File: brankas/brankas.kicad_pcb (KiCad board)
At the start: 2 copper layers, 1 part, among them SW1 SW_SPDT_XKB_DMx-xxxx-1

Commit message: Add Track
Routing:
- net unconnected-(SW1-A-Pad1): track 0.00 -> 157.9 mm
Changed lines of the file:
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@@
 		)
 	)
+	(segment
+		(start 177 78)
+		(end 208 47)
+		(width 0.2)
+		(layer "F.Cu")
+		(net 2)
+	)
+	(segment
+		(start 137.5 36.5)
+		(end 119 55)
+		(width 0.2)
+		(layer "F.Cu")
+		(net 2)
+	)
+	(segment
+		(start 164 78)
+		(end 177 78)
+		(width 0.2)
+		(layer "F.Cu")
+		(net 2)
+	)
+	(segment
+		(start 197.5 36.5)
+		(end 173.5 36.5)
+		(width 0.2)
+		(layer "F.Cu")
+		(net 2)
+	)
+	(segment
+		(start 173.5 36.5)
+		(end 137.5 36.5)
+		(width 0.2)
+		(layer "F.Cu")
+		(net 2)
+	)
+	(segment
+		(start 208 47)
+		(end 197.5 36.5)
+		(width 0.2)
+		(layer "F.Cu")
+		(net 2)
+	)
 )

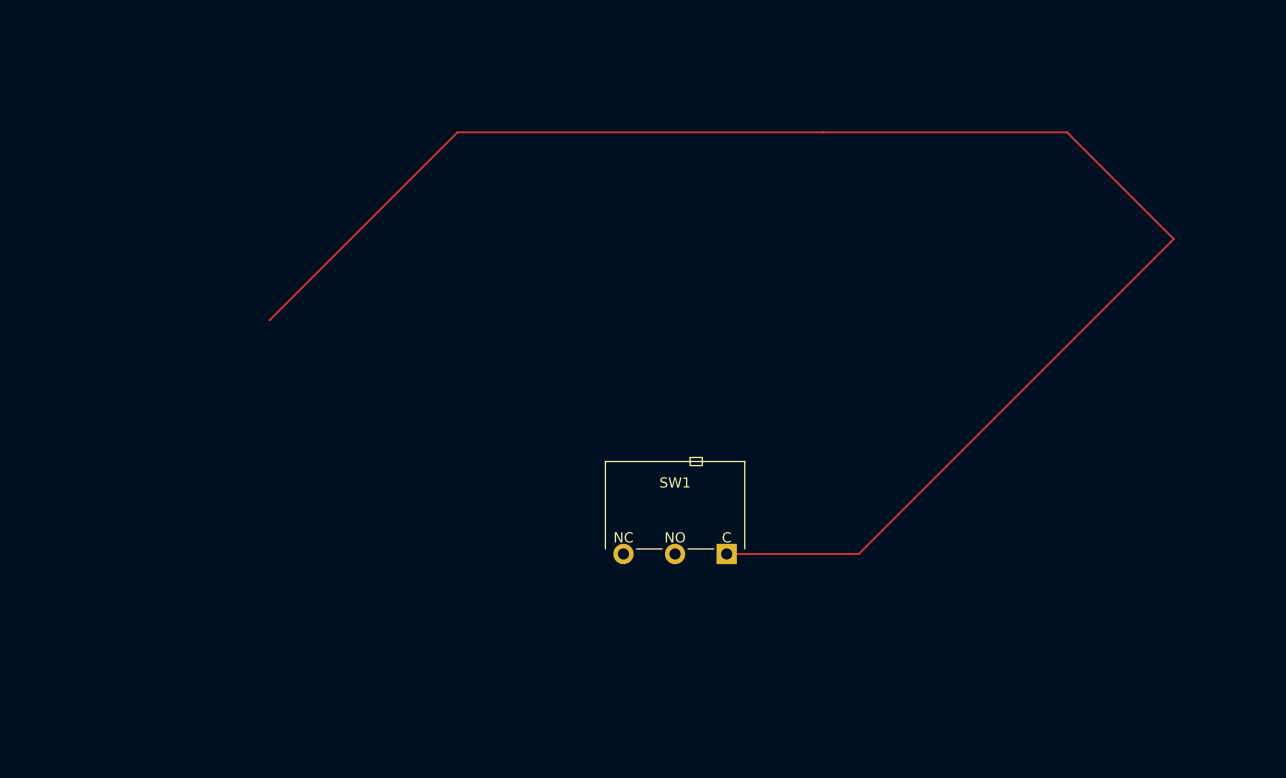
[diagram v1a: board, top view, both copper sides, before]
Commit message: Button added & Outline revision
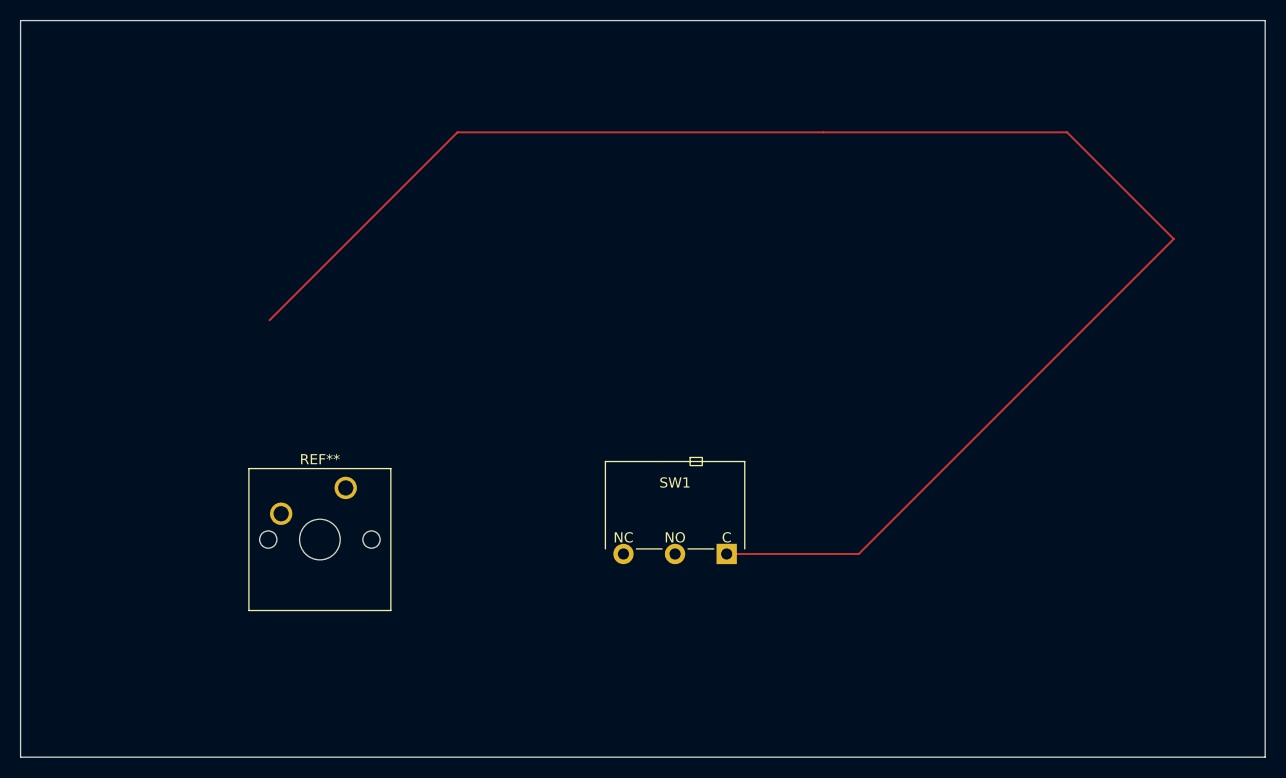
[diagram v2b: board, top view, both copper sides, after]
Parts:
- added REF**: SW_Cherry_MX_1.00u_PCB, Button_Switch_Keyboard:SW_Cherry_MX_1.00u_PCB, F.Cu at (126.5, 71.5)
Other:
- board outline added: 122.5 x 72.5 mm
